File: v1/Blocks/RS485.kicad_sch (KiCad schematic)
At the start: 6 parts, among them IC47 SN65HVD75DR, J10 Conn_02x01, J9 Conn_02x01

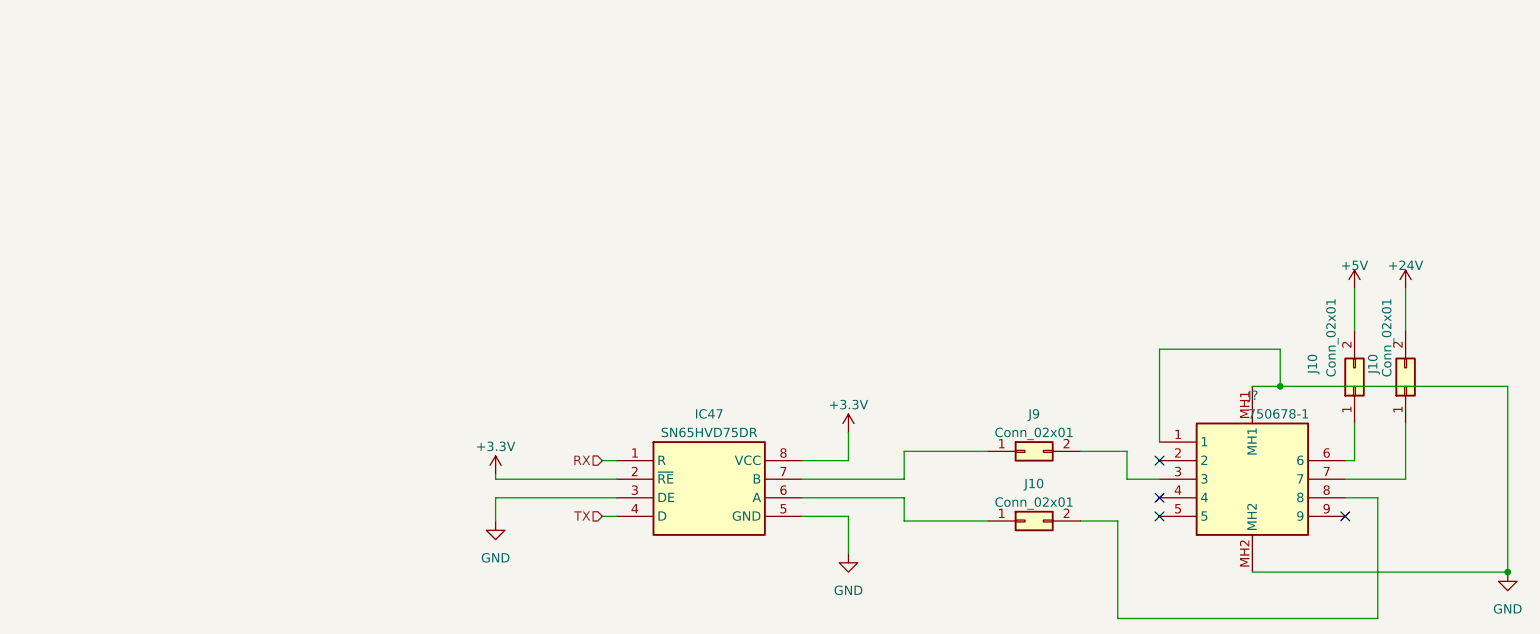
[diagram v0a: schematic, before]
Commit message: Update views, to make drawing sheets smaller where necessary
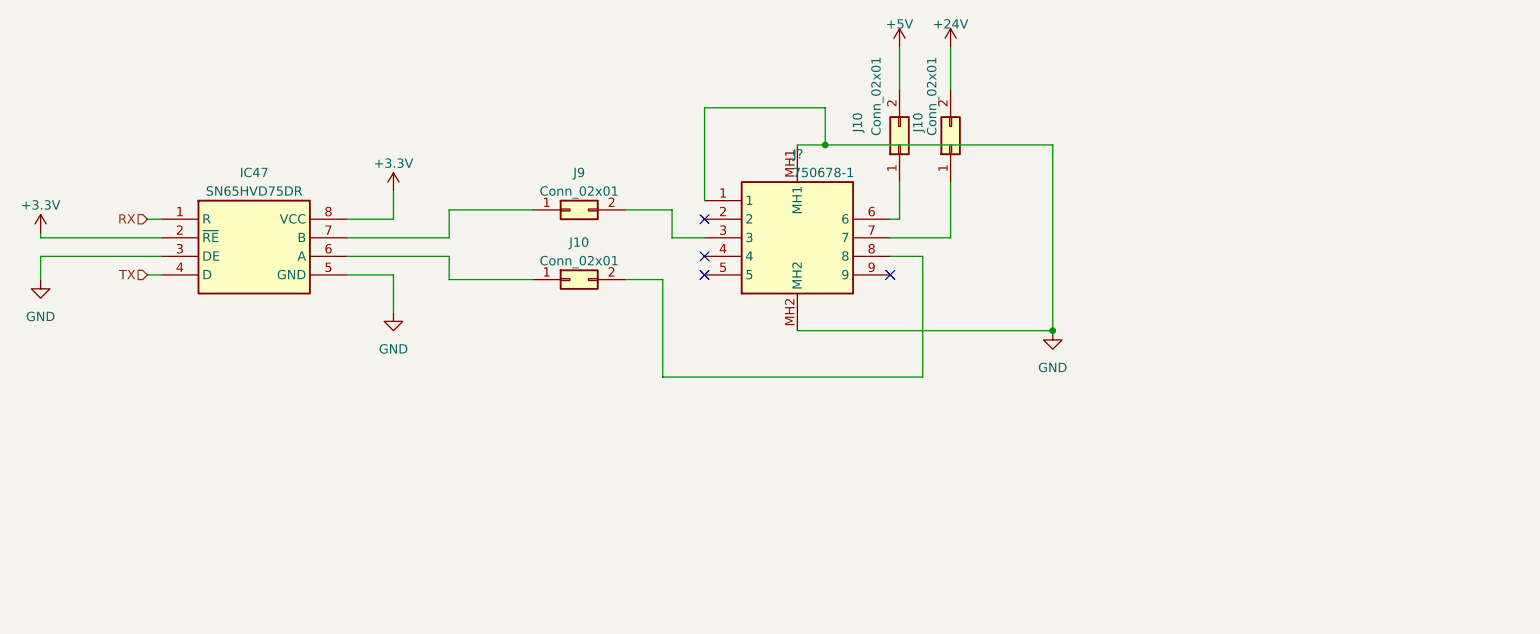
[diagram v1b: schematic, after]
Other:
- moved on the sheet: IC47, J10, J9, J?
